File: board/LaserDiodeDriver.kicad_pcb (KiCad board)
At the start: 2 copper layers, 55 parts, among them J1 Conn_01x02, K1 EE2-12NU, Q1 2N7002, Q2 IRF9Z34, SW1 SW_SPDT, U1 LT1009, U2 OPA4192, U3 LM317_TO-220

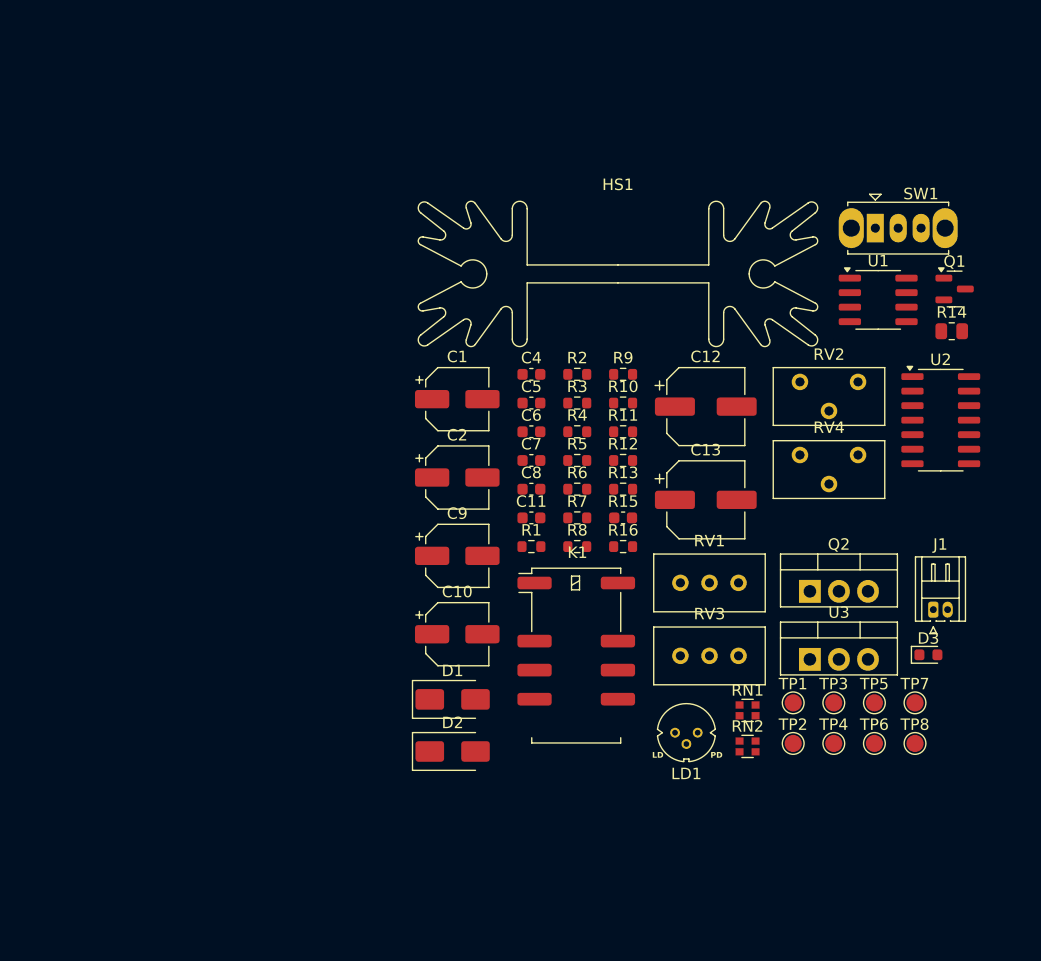
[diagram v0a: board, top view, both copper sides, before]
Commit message: Set height of objects and began rough layout
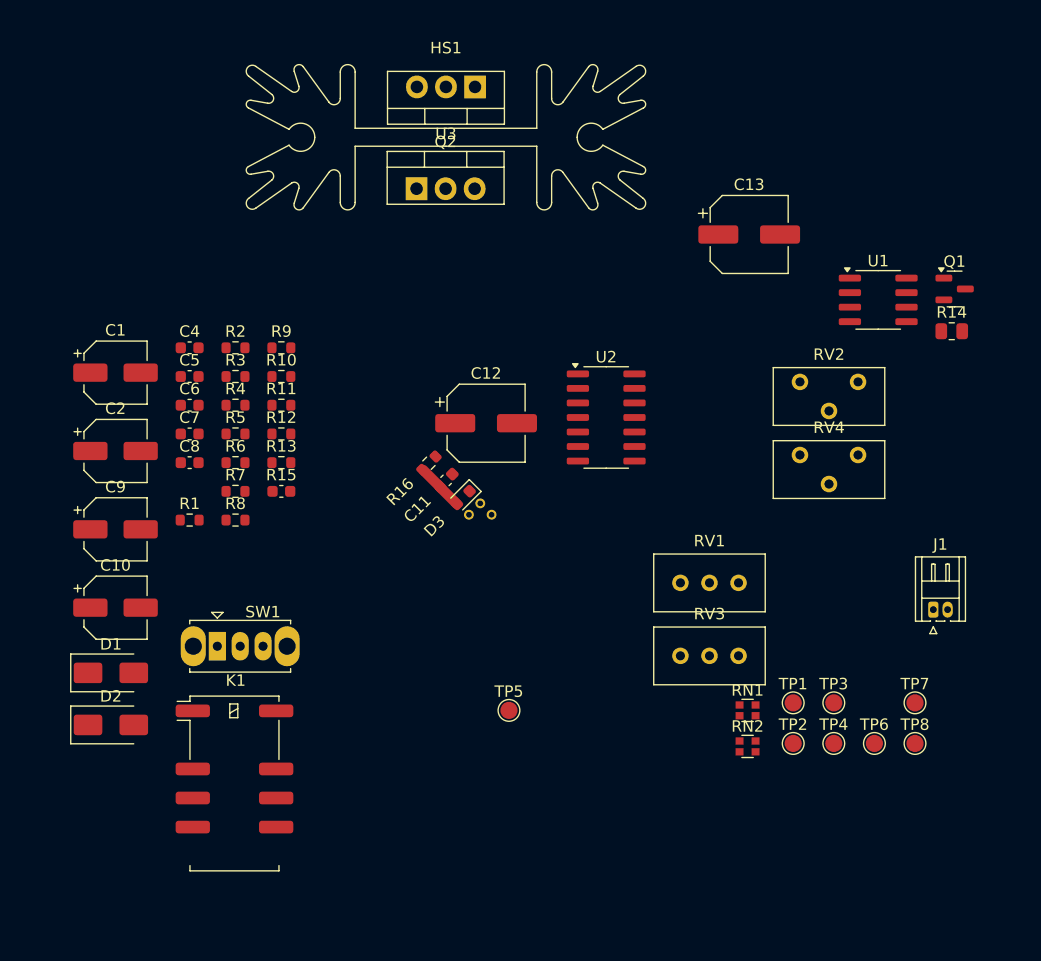
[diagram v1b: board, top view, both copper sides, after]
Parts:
- LD1: moved to B.Cu
- moved SW1 68.2 mm to (131.0, 107.0)
- moved U3 58.0 mm to (153.5, 58.1), turned to 180 degrees
- moved Q2 49.2 mm to (148.4, 67.0)
- moved D3 42.9 mm to (152.5, 94.0), turned to -135 degrees
- moved TP5 32.0 mm to (156.5, 112.6)
- moved K1 31.9 mm to (132.5, 119.0)
- moved C1 30.0 mm to (122.1, 83.1)
- moved C10 30.0 mm to (122.1, 103.6)
- moved C2 30.0 mm to (122.1, 89.9)
- moved C4 30.0 mm to (128.6, 80.9)
- moved C5 30.0 mm to (128.6, 83.4)
- moved C6 30.0 mm to (128.6, 85.9)
- moved C7 30.0 mm to (128.6, 88.4)
- moved C8 30.0 mm to (128.6, 91.0)
- moved C9 30.0 mm to (122.1, 96.8)
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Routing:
- net Net-(D3-A2): track 0.00 -> 4.38 mm

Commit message: Shunt Sense footprint
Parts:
- R14: footprint Resistor_SMD:R_0805_2012Metric -> LD_Library:R_Shunt_0805_2012Metric
- moved R14 37.3 mm to (161.5, 95.5)
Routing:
- net Net-(RN1B-R2.1): track 0.00 -> 2.45 mm, vias 0 -> 1
- net Net-(D3-A2): track 4.38 -> 6.79 mm, vias 0 -> 1
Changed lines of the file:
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@@
 		)
 	)
-	(footprint "Resistor_SMD:R_0805_2012Metric"
+	(footprint "LD_Library:R_Shunt_0805_2012Metric"
 		(layer "F.Cu")
-		(at 195.21 79.46)
-		(descr "Resistor SMD 0805 (2012 Metric), square (rectangular) end terminal, IPC-7351 nominal, (Body size source: IPC-SM-782 page 72, https://www.pcb-3d.com/wordpress/wp-content/uploads/ipc-sm-782a_amendment_1_and_2.pdf), generated with kicad-footprint-generator")
-		(tags "resistor")
+		(at 161.5 95.5)
 		(property "Reference" "R14"
-			(at 0 -1.65 0)
+			(at -0.05 2.1 0)
+			(unlocked yes)
 			(layer "F.SilkS")
 			(effects
@@
 		)
 		(property "Value" "1Ω±0.25%, 1/8W"
-			(at 0 1.65 0)
+			(at -0.05 3.6 0)
+			(unlocked yes)
 			(layer "F.Fab")
 			(effects
@@
 		(property "Datasheet" "https://www.digikey.com/en/products/detail/bourns-inc/CRT0805-CY-1R00ELF/2564154"
 			(at 0 0 0)
+			(unlocked yes)
 			(layer "F.Fab")
 			(hide yes)
 			(effects
 				(font
-					(size 1.27 1.27)
+					(size 1 1)
 					(thickness 0.15)
 				)
@@
 		(property "Description" "1 Ohms ±0.25% 0.125W, 1/8W Chip Resistor 0805 (2012 Metric) Current Sense Thin Film"
 			(at 0 0 0)
+			(unlocked yes)
 			(layer "F.Fab")
 			(hide yes)
 			(effects
 				(font
-					(size 1.27 1.27)
+					(size 1 1)
 					(thickness 0.15)
 				)
@@
 		)
 		(fp_line
-			(start -1.68 -0.95)
-			(end 1.68 -0.95)
+			(start -2 -0.95)
+			(end 2.05 -0.95)
 			(stroke
 				(width 0.05)
@@
 		)
 		(fp_line
-			(start -1.68 0.95)
-			(end -1.68 -0.95)
+			(start -2 0.95)
+			(end -2 -0.95)
 			(stroke
 				(width 0.05)
@@
 		)
 		(fp_line
-			(start 1.68 -0.95)
-			(end 1.68 0.95)
+			(start 2.05 -0.95)
+			(end 2.05 0.95)
 			(stroke
 				(width 0.05)
@@
 		)
 		(fp_line
-			(start 1.68 0.95)
-			(end -1.68 0.95)
+			(start 2.05 0.95)
+			(end -2 0.95)
 			(stroke
 				(width 0.05)
@@
 		)
 		(fp_text user "${REFERENCE}"
-			(at 0 0 0)
+			(at -0.05 5.1 0)
+			(unlocked yes)
 			(layer "F.Fab")
 			(effects
 				(font
-					(size 0.5 0.5)
-					(thickness 0.08)
+					(size 1 1)
+					(thickness 0.15)
 				)
 			)
 		)
 		(pad "1" smd roundrect
-			(at -0.9125 0)
-			(size 1.025 1.4)
+			(at -0.9125 -0.475)
+			(size 1.025 0.45)
+			(layers "F.Cu" "F.Mask" "F.Paste")
+			(roundrect_rratio 0.243902)
+			(net 23 "Net-(Q2-D)")
+			(pintype "passive")
+		)
+		(pad "1" smd roundrect
+			(at -0.9125 0.5)
+			(size 1.025 0.4)
 			(layers "F.Cu" "F.Mask" "F.Paste")
 			(roundrect_rratio 0.243902)
@@
 		)
 		(pad "2" smd roundrect
-			(at 0.9125 0)
-			(size 1.025 1.4)
+			(at 0.90625 0.5)
+			(size 1.0375 0.4)
 			(layers "F.Cu" "F.Mask" "F.Paste")
 			(roundrect_rratio 0.243902)
@@
 			(pintype "passive")
 		)
-		(embedded_fonts no)
-		(model "${KICAD9_3DMODEL_DIR}/Resistor_SMD.3dshapes/R_0805_2012Metric.step"
-			(offset
-				(xyz 0 0 0)
-			)
-			(scale
-				(xyz 1 1 1)
-			)
-			(rotate
-				(xyz 0 0 0)
-			)
+		(pad "2" smd roundrect
+			(at 0.9125 -0.475)
+			(size 1.025 0.45)
+			(layers "F.Cu" "F.Mask" "F.Paste")
+			(roundrect_rratio 0.243902)
+			(net 27 "Net-(RN1A-R1.2)")
+			(pintype "passive")
+		)
+		(pad "3" smd roundrect
+			(at 0.9125 0.009375 90)
+			(size 0.28125 0.975)
+			(layers "F.Cu" "F.Mask" "F.Paste")
+			(roundrect_rratio 0.243902)
+			(net 30 "Net-(RN1B-R2.1)")
+			(pintype "passive")
+		)
+		(pad "4" smd roundrect
+			(at -0.90625 0.009375 90)
+			(size 0.28125 1.0125)
+			(layers "F.Cu" "F.Mask" "F.Paste")
+			(roundrect_rratio 0.243902)
+			(net 13 "Net-(D3-A2)")
+			(pintype "passive")
 		)
+		(embedded_fonts no)
 	)
 	(footprint "Package_SO:SOIC-14_3.9x8.7mm_P1.27mm"
@@
 	)
 	(segment
+		(start 161.235677 95.509375)
+		(end 161.247558 95.521256)
+		(width 0.1)
+		(layer "F.Cu")
+		(net 13)
+	)
+	(segment
 		(start 151.943153 94.556847)
 		(end 150.451992 93.065686)
@@
 	)
 	(segment
+		(start 160.3625 95.509375)
+		(end 160.353125 95.5)
+		(width 0.1)
+		(layer "F.Cu")
+		(net 13)
+	)
+	(segment
+		(start 160.59375 95.509375)
+		(end 161.235677 95.509375)
+		(width 0.1)
+		(layer "F.Cu")
+		(net 13)
+	)
+	(segment
 		(start 148.987347 91.583363)
 		(end 150.451992 93.048008)
@@
 		(net 13)
 	)
+	(via micro
+		(at 161.247558 95.521256)
+		(size 0.3)
+		(drill 0.1)
+		(layers "F.Cu" "B.Cu")
+		(net 13)
+	)
+	(segment
+		(start 161.247558 95.521256)
+		(end 161.247558 97.252442)
+		(width 0.1)
+		(layer "B.Cu")
+		(net 13)
+	)
+	(segment
+		(start 162.4125 95.509375)
+		(end 161.75616 95.509375)
+		(width 0.1)
+		(layer "F.Cu")
+		(net 30)
+	)
+	(segment
+		(start 162.6875 95.509375)
+		(end 162.696875 95.5)
+		(width 0.1)
+		(layer "F.Cu")
+		(net 30)
+	)
+	(segment
+		(start 161.75616 95.509375)
+		(end 161.747548 95.517987)
+		(width 0.1)
+		(layer "F.Cu")
+		(net 30)
+	)
+	(via micro
+		(at 161.747548 95.517987)
+		(size 0.3)
+		(drill 0.1)
+		(layers "F.Cu" "B.Cu")
+		(net 30)
+	)
+	(segment
+		(start 161.747548 95.517987)
+		(end 161.747548 97.286312)
+		(width 0.1)
+		(layer "B.Cu")
+		(net 30)
+	)
 	(embedded_fonts no)

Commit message: Trying goofy layout things
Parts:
- moved C7 34.4 mm to (159.5, 103.5), turned to 180 degrees
- moved R9 31.1 mm to (159.5, 102.0), turned to 180 degrees
- moved RN2 29.4 mm to (150.0, 105.0), turned to -90 degrees
- moved RV1 26.0 mm to (186.6, 125.5)
- moved RN1 24.8 mm to (154.5, 103.0), turned to 180 degrees
- moved U2 22.7 mm to (156.3, 108.0), turned to -90 degrees
- moved RV3 17.4 mm to (171.6, 124.5)
- moved R14 10.5 mm to (151.0, 95.5), turned to -90 degrees
- moved C11 7.21 mm to (147.0, 86.5)
- moved C12 7.21 mm to (150.5, 81.5)
- moved D3 7.21 mm to (148.5, 88.0)
- moved R16 7.21 mm to (145.5, 85.0)
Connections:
- C1 pad 1: Net-(U2A-+) -> Net-(U2D-+)
- C13 pad 1: Net-(U2B-+) -> Net-(U2C-+)
- C4 pad 1: Net-(U2A--) -> Net-(U2D--)
- C5 pad 1: Net-(U2B--) -> Net-(U2C--)
- C7 pad 2: Net-(U2D--) -> Net-(U2A--)
- LD1 pad 1: Net-(U2D--) -> Net-(U2A--)
- R2 pad 2: Net-(U2A-+) -> Net-(U2D-+)
- R4 pad 2: Net-(U2B--) -> Net-(U2C--)
- R5 pad 2: Net-(U2B-+) -> Net-(U2C-+)
- R6 pad 1: Net-(U2A--) -> Net-(U2D--)
- R9 pad 2: Net-(U2D--) -> Net-(U2A--)
- RN2 pad 1: Net-(RN1A-R1.1) -> V_{I_LD}
- RN2 pad 2: GND -> Net-(RN1B-R2.2)
- RN2 pad 3: V_{I_LD} -> GND
- RN2 pad 4: Net-(RN1B-R2.2) -> Net-(RN1A-R1.1)
- U2 pad 1: v_{ref} -> V_{P_PD}
- U2 pad 10: Net-(RN1A-R1.1) -> Net-(U2C-+)
- U2 pad 12: v_{ref} -> Net-(U2D-+)
- U2 pad 14: V_{P_PD} -> v_{ref}
- U2 pad 3: Net-(U2A-+) -> v_{ref}
- U2 pad 5: Net-(U2B-+) -> Net-(RN1A-R1.1)
- U2 pad 6: Net-(U2B--) -> Net-(RN1B-R2.2)
- U2 pad 7: Net-(C5-Pad2) -> V_{I_LD}
- U2 pad 8: V_{I_LD} -> Net-(C5-Pad2)
- U2 pad 9: Net-(RN1B-R2.2) -> Net-(U2C--)
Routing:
- net Net-(RN1A-R1.1): track 0.00 -> 8.22 mm
- net Net-(RN1B-R2.2): track 0.00 -> 7.13 mm
- net Net-(D3-A2): track 6.79 -> 0.00 mm, vias 1 -> 0
- net Net-(U2A--): track 0.00 -> 3.58 mm
- net V_{P_PD}: track 0.00 -> 3.56 mm
- net V_{I_LD}: track 0.00 -> 2.56 mm
- net Net-(RN1B-R2.1): track 2.45 -> 0.00 mm, vias 1 -> 0
- added copper zone on B.Cu, net GND
